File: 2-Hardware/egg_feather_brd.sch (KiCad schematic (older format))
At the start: 6 parts

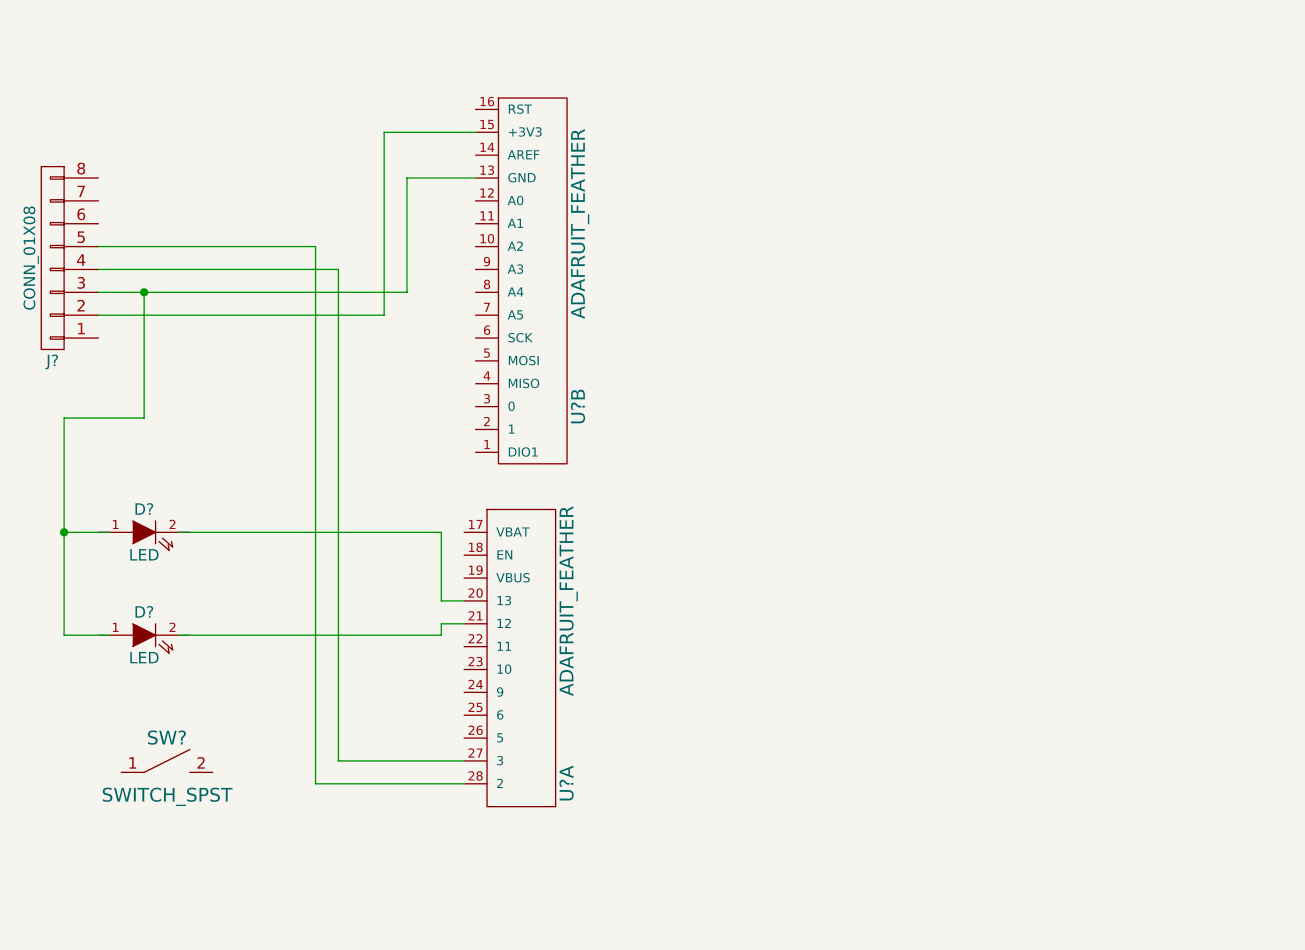
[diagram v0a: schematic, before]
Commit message: Changed to BOB circuit
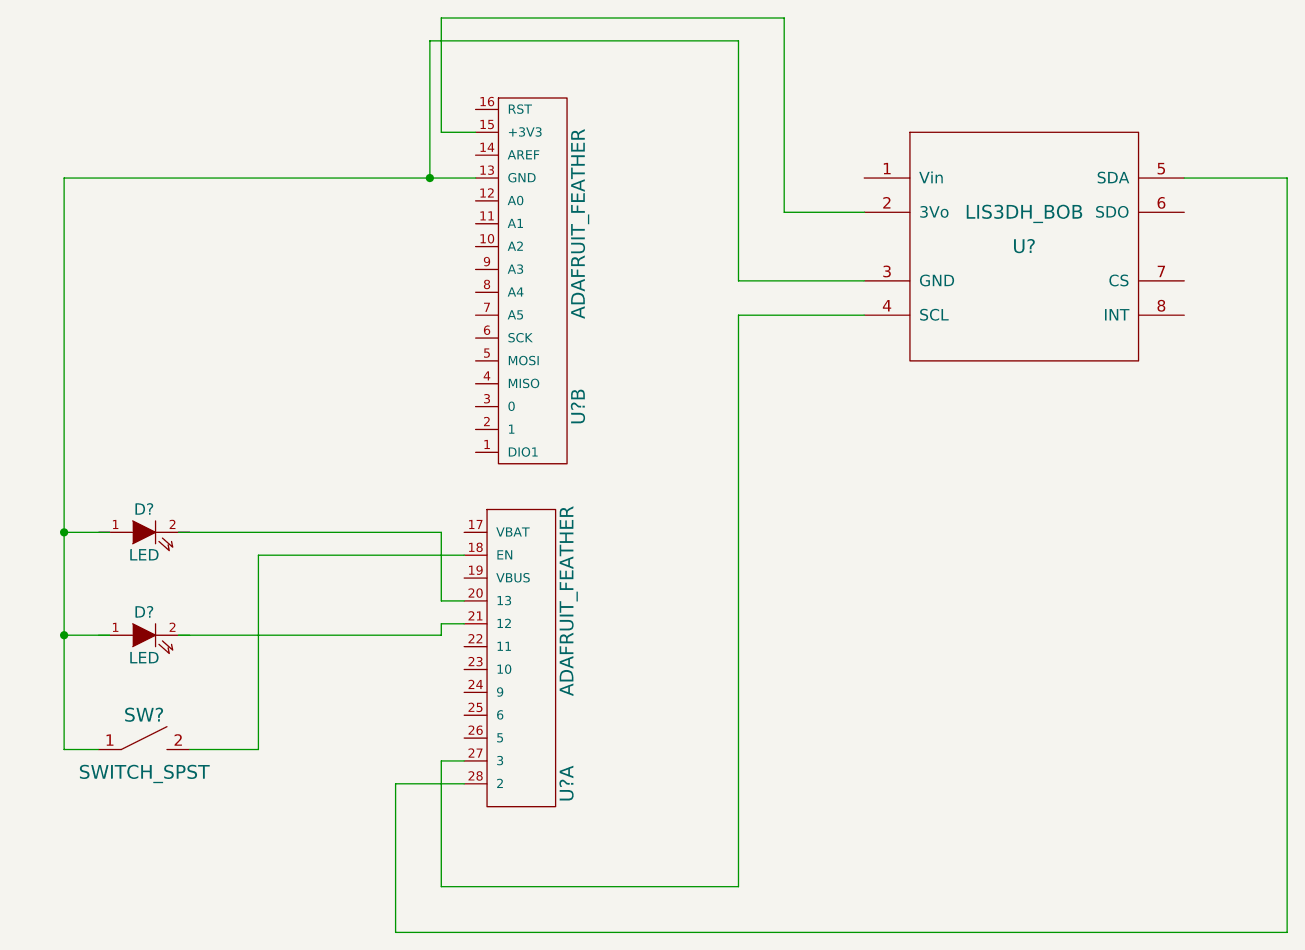
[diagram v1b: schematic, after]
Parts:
- removed J?: CONN_01X08, symbol CONN_01X08
- added U?: LIS3DH_BOB, symbol LIS3DH_BOB
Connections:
- wire segments 23 -> 33
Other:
- moved on the sheet: SW?
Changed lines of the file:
@@
 LIBS:contrib
 LIBS:valves
-LIBS:MiscellaneousDevices
-LIBS:Sensors
+LIBS:egg_feather_brd-cache
 EELAYER 25 0
 EELAYER END
@@
 $EndComp
 $Comp
-L CONN_01X08 J?
-U 1 1 5955C7DA
-P 4500 3050
-F 0 "J?" H 4500 3500 50  0000 C CNN
-F 1 "CONN_01X08" V 4600 3050 50  0000 C CNN
-F 2 "" H 4500 3050 50  0001 C CNN
-F 3 "" H 4500 3050 50  0001 C CNN
-	1    4500 3050
-	-1   0    0    1
-$EndComp
-$Comp
 L LED D?
 U 1 1 5955CFB2
@@
 L SWITCH_SPST SW?
 U 1 1 5955E018
-P 5000 5300
-F 0 "SW?" H 5000 5450 60  0000 C CNN
-F 1 "SWITCH_SPST" H 5000 5200 60  0000 C CNN
-F 2 "" H 5000 5300 60  0000 C CNN
-F 3 "" H 5000 5300 60  0000 C CNN
-	1    5000 5300
+P 4900 5200
+F 0 "SW?" H 4900 5350 60  0000 C CNN
+F 1 "SWITCH_SPST" H 4900 5100 60  0000 C CNN
+F 2 "" H 4900 5200 60  0000 C CNN
+F 3 "" H 4900 5200 60  0000 C CNN
+	1    4900 5200
 	1    0    0    -1
 $EndComp
-Wire Wire Line
-	4700 3300 5950 3300
-Wire Wire Line
-	5950 3300 5950 2500
-Wire Wire Line
-	5950 2500 6350 2500
-Wire Wire Line
-	4700 3200 6050 3200
-Wire Wire Line
-	6050 3200 6050 2700
-Wire Wire Line
-	6050 2700 6350 2700
-Wire Wire Line
-	4700 3100 5750 3100
-Wire Wire Line
-	5750 3100 5750 5250
-Wire Wire Line
-	5750 5250 6300 5250
-Wire Wire Line
-	4700 3000 5650 3000
-Wire Wire Line
-	5650 3000 5650 5350
-Wire Wire Line
-	5650 5350 6300 5350
 Wire Wire Line
 	5050 4250 6200 4250
@@
 	4750 4250 4550 4250
 Wire Wire Line
-	4550 3750 4550 4700
-Wire Wire Line
-	4550 3750 4900 3750
-Wire Wire Line
-	4900 3750 4900 3200
-Connection ~ 4900 3200
+	4550 2700 4550 5200
 Wire Wire Line
 	4550 4700 4750 4700
 Connection ~ 4550 4250
+Wire Wire Line
+	6300 4350 5400 4350
+Wire Wire Line
+	5400 4350 5400 5200
+Wire Wire Line
+	5400 5200 5100 5200
+Wire Wire Line
+	4550 5200 4700 5200
+Connection ~ 4550 4700
+$Comp
+L LIS3DH_BOB U?
+U 1 1 595FB4D9
+P 8750 3000
+F 0 "U?" H 8750 3000 60  0000 C CNN
+F 1 "LIS3DH_BOB" H 8750 3150 60  0000 C CNN
+F 2 "" H 8750 3000 60  0001 C CNN
+F 3 "" H 8750 3000 60  0001 C CNN
+	1    8750 3000
+	1    0    0    -1
+$EndComp
+Wire Wire Line
+	8050 2850 7700 2850
+Wire Wire Line
+	7700 2850 7700 2000
+Wire Wire Line
+	7700 2000 6200 2000
+Wire Wire Line
+	6200 2000 6200 2500
+Wire Wire Line
+	6200 2500 6350 2500
+Wire Wire Line
+	8050 3150 7500 3150
+Wire Wire Line
+	7500 3150 7500 2100
+Wire Wire Line
+	7500 2100 6150 2100
+Wire Wire Line
+	6150 2100 6150 2700
+Wire Wire Line
+	4550 2700 6350 2700
+Wire Wire Line
+	8050 3300 7500 3300
+Wire Wire Line
+	7500 3300 7500 5800
+Wire Wire Line
+	7500 5800 6200 5800
+Wire Wire Line
+	6200 5800 6200 5250
+Wire Wire Line
+	6200 5250 6300 5250
+Wire Wire Line
+	9450 2700 9900 2700
+Wire Wire Line
+	9900 2700 9900 6000
+Wire Wire Line
+	9900 6000 6000 6000
+Wire Wire Line
+	6000 6000 6000 5350
+Wire Wire Line
+	6000 5350 6300 5350
+Connection ~ 6150 2700
 $EndSCHEMATC
